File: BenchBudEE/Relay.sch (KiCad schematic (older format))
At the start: 11 parts

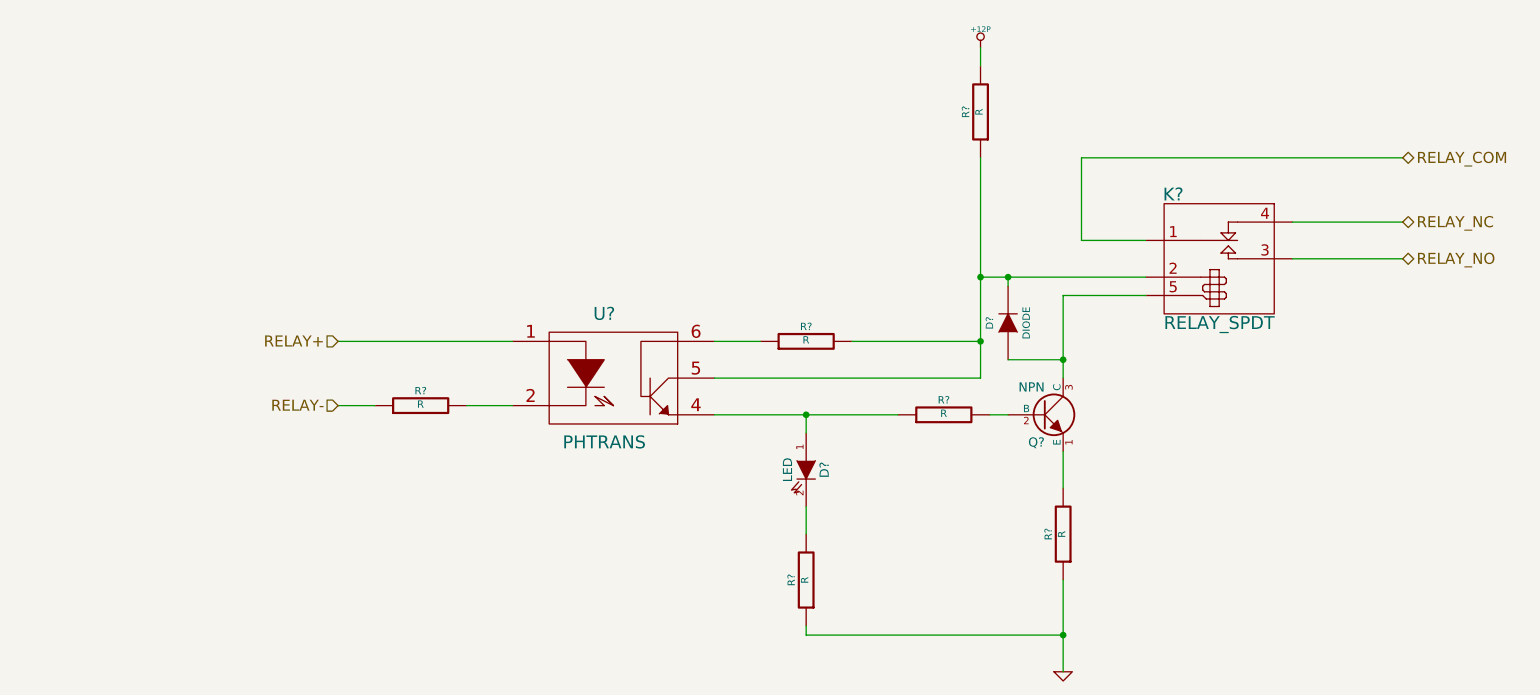
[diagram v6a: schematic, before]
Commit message: Parts added to relay module. Schematic tidied up.
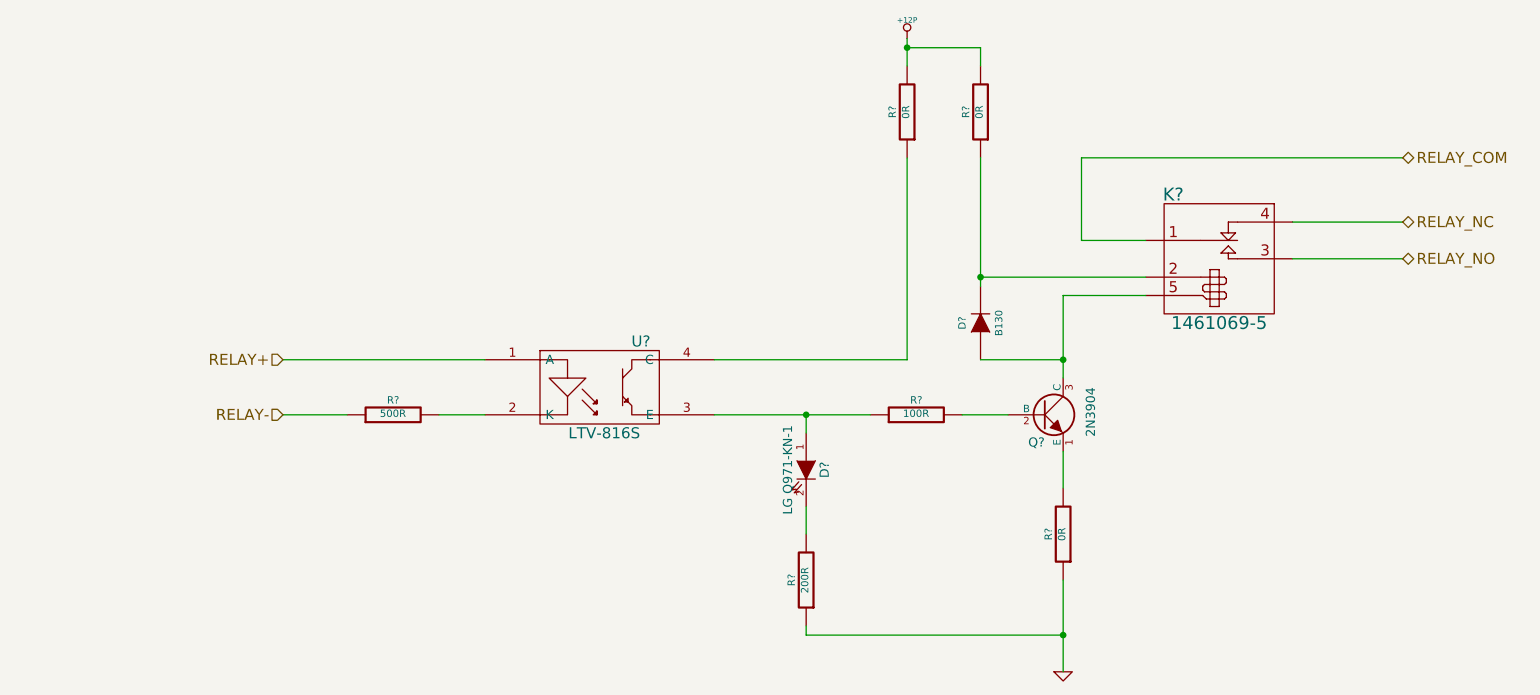
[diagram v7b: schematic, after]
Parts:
- removed R?: R, ~, symbol R
- removed U?: PHTRANS, ~, symbol PHTRANS
- added R?: 0R, ~, symbol R
- added U?: LTV-816S, symbol OPTO-TRANSISTOR4
- D?: value LED -> LG Q971-KN-1; Distributor (none) -> DigiKey; Distributor Part Link (none) -> http://www.digikey.com/product-detail/en/LG%20Q971-KN-1/475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; Distributor Part Number (none) -> 475-1409-1-ND; MFG Name (none) -> OSRAM Opto Semiconductors Inc; MFG Part Number (none) -> LG Q971-KN-1
- D?: value DIODE -> B130; Distributor (none) -> DigiKey; Distributor Part Link (none) -> http://www.digikey.com/product-detail/en/B130-13-F/B130-FDI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; Distributor Part Number (none) -> B130-FDICT-ND; MFG Name (none) -> Diodes Incorporated; MFG Part Number (none) -> B130-13-F
- K?: value RELAY_SPDT -> 1461069-5; Distributor (none) -> DigiKey; Distributor Part Link (none) -> http://www.digikey.com/product-detail/en/1461069-5/PB1321-N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; Distributor Part Number (none) -> PB1321-ND; MFG Name (none) -> TE Connectivity; MFG Part Number (none) -> 1461069-5
- Q?: value NPN -> 2N3904; Distributor (none) -> DigiKey; Distributor Part Link (none) -> http://www.digikey.com/product-detail/en/MMBT3904-7-F/MMBT3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; Distributor Part Number (none) -> MMBT3904-FDICT-ND; MFG Name (none) -> Diodes Incorporated; MFG Part Number (none) -> MMBT3904-7-F
- R?: value R -> 100R
- R? (x2): value R -> 0R
- R?: value R -> 200R
- R?: value R -> 500R
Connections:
- net +12P: now also R?.2
- net RELAY+: now also U?.1 (A)
- net at D?.1 (A), R?.1: now also U?.3 (E)
- net at R?.2: now also U?.2 (K)
- new net: R?.1, U?.4 (C)
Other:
- moved on the sheet: D?, R?
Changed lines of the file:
@@
 Sheet 2 9
 Title ""
-Date "8 feb 2014"
+Date "19 feb 2014"
 Rev ""
 Comp ""
@@
 Comment4 ""
 $EndDescr
-Text HLabel 3500 3550 0    60   Input ~ 0
+Text HLabel 3200 3650 0    60   Input ~ 0
 RELAY+
-Text HLabel 3500 3900 0    60   Input ~ 0
+Text HLabel 3200 3950 0    60   Input ~ 0
 RELAY-
 Text HLabel 9300 3100 2    60   BiDi ~ 0
@@
 RELAY_NC
 $Comp
-L PHTRANS U?
-U 1 1 52F2AEFF
-P 5000 3750
-F 0 "U?" H 4950 4100 70  0000 C CNN
-F 1 "PHTRANS" H 4950 3400 70  0000 C CNN
-F 2 "~" H 5000 3750 60  0000 C CNN
-F 3 "~" H 5000 3750 60  0000 C CNN
-	1    5000 3750
-	1    0    0    -1
-$EndComp
-$Comp
 L RELAY_SPDT K?
 U 1 1 52F29F66
 P 8300 3100
 F 0 "K?" H 8050 3450 70  0000 C CNN
-F 1 "RELAY_SPDT" H 8300 2750 70  0000 C CNN
+F 1 "1461069-5" H 8300 2750 70  0000 C CNN
 F 2 "~" H 8300 3250 60  0000 C CNN
-F 3 "~" H 8300 3250 60  0000 C CNN
+F 3 "http://media.digikey.com/pdf/Data%20Sheets/Tyco%20Electronics%20P%20B%20PDFs/ORWH.pdf" H 8300 3250 60  0001 C CNN
+F 4 "TE Connectivity" H 8300 3100 60  0001 C CNN "MFG Name"
+F 5 "1461069-5" H 8300 3100 60  0001 C CNN "MFG Part Number"
+F 6 "DigiKey" H 8300 3100 60  0001 C CNN "Distributor"
+F 7 "PB1321-ND" H 8300 3100 60  0001 C CNN "Distributor Part Number"
+F 8 "http://www.digikey.com/product-detail/en/1461069-5/PB1321-ND/3318145" H 8300 3100 60  0001 C CNN "Distributor Part Link"
 	1    8300 3100
 	1    0    0    -1
@@
 L R R?
 U 1 1 52F29F75
-P 6800 3950
-F 0 "R?" V 6880 3950 40  0000 C CNN
-F 1 "R" V 6807 3951 40  0000 C CNN
-F 2 "~" V 6730 3950 30  0000 C CNN
-F 3 "~" H 6800 3950 30  0000 C CNN
-	1    6800 3950
+P 6650 3950
+F 0 "R?" V 6730 3950 40  0000 C CNN
+F 1 "100R" V 6657 3951 40  0000 C CNN
+F 2 "~" V 6580 3950 30  0000 C CNN
+F 3 "~" H 6650 3950 30  0000 C CNN
+	1    6650 3950
 	0    -1   -1   0
 $EndComp
@@
 P 7350 3950
 F 0 "Q?" H 7350 3800 50  0000 R CNN
-F 1 "NPN" H 7350 4100 50  0000 R CNN
+F 1 "2N3904" V 7600 4100 50  0000 R CNN
 F 2 "~" H 7350 3950 60  0000 C CNN
-F 3 "~" H 7350 3950 60  0000 C CNN
+F 3 "http://www.diodes.com/datasheets/ds30036.pdf" H 7350 3950 60  0001 C CNN
+F 4 "Diodes Incorporated" H 7350 3950 60  0001 C CNN "MFG Name"
+F 5 "MMBT3904-7-F" H 7350 3950 60  0001 C CNN "MFG Part Number"
+F 6 "DigiKey" H 7350 3950 60  0001 C CNN "Distributor"
+F 7 "MMBT3904-FDICT-ND" H 7350 3950 60  0001 C CNN "Distributor Part Number"
+F 8 "http://www.digikey.com/product-detail/en/MMBT3904-7-F/MMBT3904-FDICT-ND/815727" H 7350 3950 60  0001 C CNN "Distributor Part Link"
 	1    7350 3950
 	1    0    0    -1
@@
 P 6050 4250
 F 0 "D?" H 6050 4350 50  0000 C CNN
-F 1 "LED" H 6050 4150 50  0000 C CNN
+F 1 "LG Q971-KN-1" H 6050 4150 50  0000 C CNN
 F 2 "~" H 6050 4250 60  0000 C CNN
-F 3 "~" H 6050 4250 60  0000 C CNN
+F 3 "http://catalog.osram-os.com/catalogue/catalogue.do;jsessionid=DE4D071D0D2758CC117C711BF848053E?act=downloadFile&favOid=0200000600005069000100b6" H 6050 4250 60  0001 C CNN
+F 4 "OSRAM Opto Semiconductors Inc" H 6050 4250 60  0001 C CNN "MFG Name"
+F 5 "LG Q971-KN-1" H 6050 4250 60  0001 C CNN "MFG Part Number"
+F 6 "DigiKey" H 6050 4250 60  0001 C CNN "Distributor"
+F 7 "475-1409-1-ND" H 6050 4250 60  0001 C CNN "Distributor Part Number"
+F 8 "http://www.digikey.com/product-detail/en/LG%20Q971-KN-1/475-1409-1-ND/1802597" H 6050 4250 60  0001 C CNN "Distributor Part Link"
 	1    6050 4250
 	0    1    1    0
@@
 P 7450 4600
 F 0 "R?" V 7530 4600 40  0000 C CNN
-F 1 "R" V 7457 4601 40  0000 C CNN
+F 1 "0R" V 7457 4601 40  0000 C CNN
 F 2 "~" V 7380 4600 30  0000 C CNN
 F 3 "~" H 7450 4600 30  0000 C CNN
@@
 P 6050 4850
 F 0 "R?" V 6130 4850 40  0000 C CNN
-F 1 "R" V 6057 4851 40  0000 C CNN
+F 1 "200R" V 6057 4851 40  0000 C CNN
 F 2 "~" V 5980 4850 30  0000 C CNN
 F 3 "~" H 6050 4850 30  0000 C CNN
@@
 $Comp
 L R R?
-U 1 1 52F2A0AD
-P 6050 3550
-F 0 "R?" V 6130 3550 40  0000 C CNN
-F 1 "R" V 6057 3551 40  0000 C CNN
-F 2 "~" V 5980 3550 30  0000 C CNN
-F 3 "~" H 6050 3550 30  0000 C CNN
-	1    6050 3550
-	0    -1   -1   0
-$EndComp
-$Comp
-L R R?
 U 1 1 52F2A0C7
 P 7000 2300
 F 0 "R?" V 7080 2300 40  0000 C CNN
-F 1 "R" V 7007 2301 40  0000 C CNN
+F 1 "0R" V 7007 2301 40  0000 C CNN
 F 2 "~" V 6930 2300 30  0000 C CNN
 F 3 "~" H 7000 2300 30  0000 C CNN
@@
 L R R?
 U 1 1 52F2A0F9
-P 3950 3900
-F 0 "R?" V 4030 3900 40  0000 C CNN
-F 1 "R" V 3957 3901 40  0000 C CNN
-F 2 "~" V 3880 3900 30  0000 C CNN
-F 3 "~" H 3950 3900 30  0000 C CNN
-	1    3950 3900
+P 3800 3950
+F 0 "R?" V 3880 3950 40  0000 C CNN
+F 1 "500R" V 3807 3951 40  0000 C CNN
+F 2 "~" V 3730 3950 30  0000 C CNN
+F 3 "~" H 3800 3950 30  0000 C CNN
+	1    3800 3950
 	0    -1   -1   0
 $EndComp
@@
 L +12P #PWR?
 U 1 1 52F2A164
-P 7000 1950
-F 0 "#PWR?" H 7000 1920 30  0001 C CNN
-F 1 "+12P" H 7000 2050 30  0000 C CNN
-F 2 "" H 7000 1950 60  0000 C CNN
-F 3 "" H 7000 1950 60  0000 C CNN
-	1    7000 1950
+P 6600 1900
+F 0 "#PWR?" H 6600 1870 30  0001 C CNN
+F 1 "+12P" H 6600 2000 30  0000 C CNN
+F 2 "" H 6600 1900 60  0000 C CNN
+F 3 "" H 6600 1900 60  0000 C CNN
+	1    6600 1900
 	1    0    0    -1
 $EndComp
@@
 L DIODE D?
 U 1 1 52F2A1DE
-P 7150 3450
-F 0 "D?" H 7150 3550 40  0000 C CNN
-F 1 "DIODE" H 7150 3350 40  0000 C CNN
-F 2 "~" H 7150 3450 60  0000 C CNN
-F 3 "~" H 7150 3450 60  0000 C CNN
-	1    7150 3450
+P 7000 3450
+F 0 "D?" H 7000 3550 40  0000 C CNN
+F 1 "B130" H 7000 3350 40  0000 C CNN
+F 2 "~" H 7000 3450 60  0000 C CNN
+F 3 "http://www.diodes.com/datasheets/ds13002.pdf" H 7000 3450 60  0001 C CNN
+F 4 "Diodes Incorporated" H 7000 3450 60  0001 C CNN "MFG Name"
+F 5 "B130-13-F" H 7000 3450 60  0001 C CNN "MFG Part Number"
+F 6 "DigiKey" H 7000 3450 60  0001 C CNN "Distributor"
+F 7 "B130-FDICT-ND" H 7000 3450 60  0001 C CNN "Distributor Part Number"
+F 8 "http://www.digikey.com/product-detail/en/B130-13-F/B130-FDICT-ND/815318" H 7000 3450 60  0001 C CNN "Distributor Part Link"
+	1    7000 3450
 	0    -1   -1   0
 $EndComp
@@
 	8700 2900 9300 2900
 Wire Wire Line
-	6050 3950 6550 3950
-Wire Wire Line
-	7050 3950 7150 3950
+	5550 3950 6400 3950
+Wire Wire Line
+	6900 3950 7150 3950
 Wire Wire Line
 	7450 4150 7450 4350
 Wire Wire Line
-	7450 3750 7450 3650
-Wire Wire Line
-	7450 3650 7450 3300
+	7450 3300 7450 3750
 Wire Wire Line
 	7450 3300 7900 3300
 Wire Wire Line
-	7900 3200 7150 3200
-Wire Wire Line
-	7150 3200 7000 3200
-Wire Wire Line
-	7000 2550 7000 3200
-Wire Wire Line
-	7000 3200 7000 3550
-Wire Wire Line
-	7000 3550 7000 3750
-Wire Wire Line
-	7450 4850 7450 5150
-Wire Wire Line
-	7450 5150 7450 5350
+	7000 3200 7900 3200
+Wire Wire Line
+	7450 4850 7450 5350
 Wire Wire Line
 	6050 4450 6050 4600
@@
 Connection ~ 7450 5150
 Wire Wire Line
-	7000 3750 5550 3750
-Connection ~ 7000 3200
-Wire Wire Line
-	5550 3550 5800 3550
-Wire Wire Line
-	6300 3550 7000 3550
-Connection ~ 7000 3550
-Wire Wire Line
-	4200 3900 4450 3900
-Wire Wire Line
-	3700 3900 3500 3900
-Wire Wire Line
-	3500 3550 4450 3550
+	4050 3950 4300 3950
+Wire Wire Line
+	3550 3950 3200 3950
 Wire Wire Line
 	7000 1950 7000 2050
@@
 	7550 3000 7900 3000
 Wire Wire Line
-	7150 3650 7450 3650
+	7000 3650 7450 3650
 Connection ~ 7450 3650
-Wire Wire Line
-	7150 3250 7150 3200
-Connection ~ 7150 3200
-Wire Wire Line
-	5550 3950 6050 3950
 Wire Wire Line
 	6050 4050 6050 3950
 Connection ~ 6050 3950
+$Comp
+L OPTO-TRANSISTOR4 U?
+U 1 1 53052DE1
+P 4950 3800
+F 0 "U?" H 5150 4050 60  0000 C CNN
+F 1 "LTV-816S" H 4950 3550 60  0000 C CNN
+F 2 "" H 4950 3800 60  0000 C CNN
+F 3 "http://optoelectronics.liteon.com/upload/download/DS-70-97-0013/P_100_LTV-816%20826%20846%20%28M,%20S,%20S-TA,%20S-TA1,%20S-TP%29%20Series.pdf" H 4950 3800 60  0001 C CNN
+F 4 "Lite-On Inc" H 4950 3800 60  0001 C CNN "MFG Name"
+F 5 "LTV-816S" H 4950 3800 60  0001 C CNN "MFG Part Number"
+F 6 "DigiKey" H 4950 3800 60  0001 C CNN "Distributor"
+F 7 "160-1361-5-ND" H 4950 3800 60  0001 C CNN "Distributor Part Number"
+F 8 "http://www.digikey.com/product-detail/en/LTV-816S/160-1361-5-ND/385831" H 4950 3800 60  0001 C CNN "Distributor Part Link"
+	1    4950 3800
+	1    0    0    -1
+$EndComp
+Wire Wire Line
+	3200 3650 4300 3650
+$Comp
+L R R?
+U 1 1 530533DD
+P 6600 2300
+F 0 "R?" V 6680 2300 40  0000 C CNN
+F 1 "0R" V 6607 2301 40  0000 C CNN
+F 2 "~" V 6530 2300 30  0000 C CNN
+F 3 "~" H 6600 2300 30  0000 C CNN
+	1    6600 2300
+	-1   0    0    1
+$EndComp
+Wire Wire Line
+	7000 1950 6600 1950
+Wire Wire Line
+	6600 1900 6600 2050
+Connection ~ 6600 1950
+Wire Wire Line
+	7000 2550 7000 3250
+Wire Wire Line
+	5550 3650 6600 3650
+Wire Wire Line
+	6600 3650 6600 2550
+Connection ~ 7000 3200
 $EndSCHEMATC

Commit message: Design rules specified for layout.
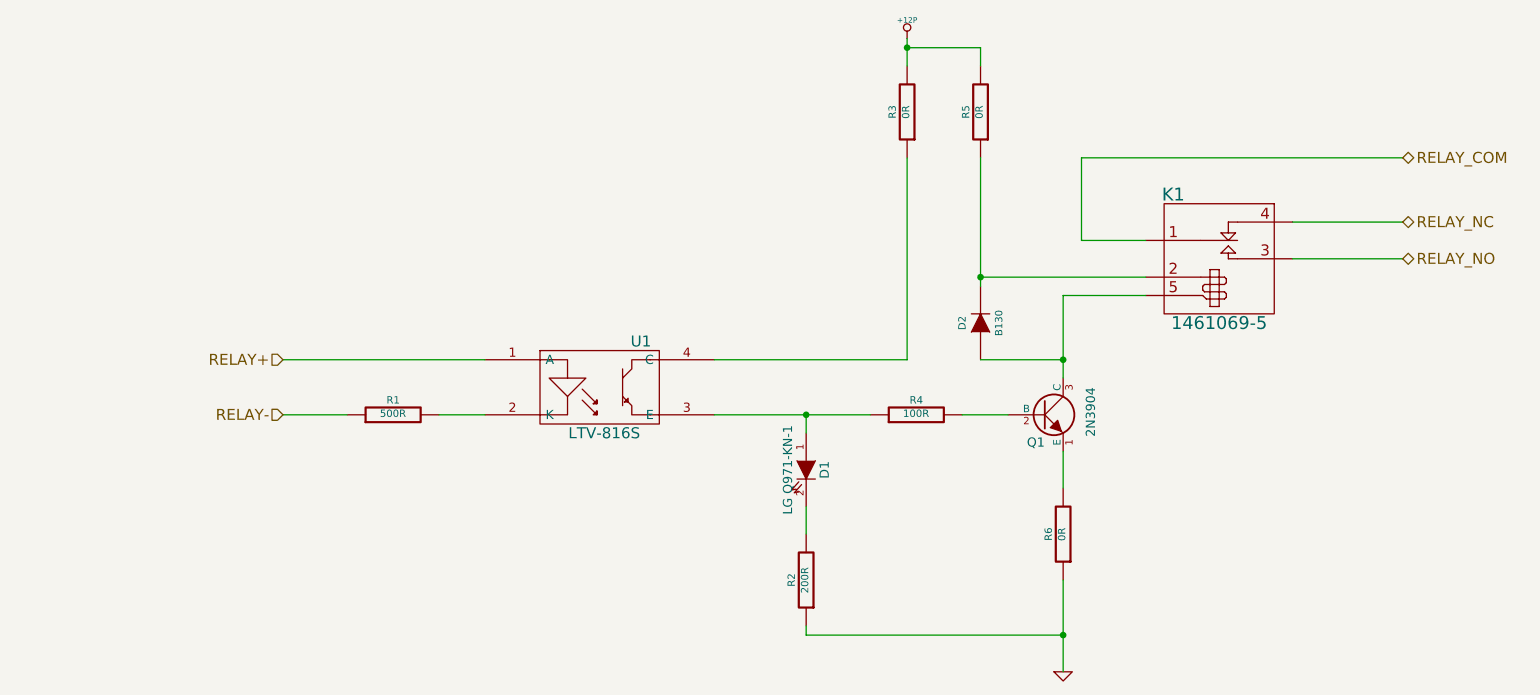
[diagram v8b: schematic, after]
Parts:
- gave numbers to parts that had none: 11
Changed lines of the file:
@@
 RELAY_NC
 $Comp
-L RELAY_SPDT K?
+L RELAY_SPDT K1
 U 1 1 52F29F66
 P 8300 3100
-F 0 "K?" H 8050 3450 70  0000 C CNN
+F 0 "K1" H 8050 3450 70  0000 C CNN
 F 1 "1461069-5" H 8300 2750 70  0000 C CNN
 F 2 "~" H 8300 3250 60  0000 C CNN
@@
 $EndComp
 $Comp
-L R R?
+L R R4
 U 1 1 52F29F75
 P 6650 3950
-F 0 "R?" V 6730 3950 40  0000 C CNN
+F 0 "R4" V 6730 3950 40  0000 C CNN
 F 1 "100R" V 6657 3951 40  0000 C CNN
 F 2 "~" V 6580 3950 30  0000 C CNN
@@
 $EndComp
 $Comp
-L NPN Q?
+L NPN Q1
 U 1 1 52F29F84
 P 7350 3950
-F 0 "Q?" H 7350 3800 50  0000 R CNN
+F 0 "Q1" H 7350 3800 50  0000 R CNN
 F 1 "2N3904" V 7600 4100 50  0000 R CNN
 F 2 "~" H 7350 3950 60  0000 C CNN
@@
 $EndComp
 $Comp
-L LED D?
+L LED D1
 U 1 1 52F29F93
 P 6050 4250
-F 0 "D?" H 6050 4350 50  0000 C CNN
+F 0 "D1" H 6050 4350 50  0000 C CNN
 F 1 "LG Q971-KN-1" H 6050 4150 50  0000 C CNN
 F 2 "~" H 6050 4250 60  0000 C CNN
@@
 RELAY_COM
 $Comp
-L R R?
+L R R6
 U 1 1 52F2A010
 P 7450 4600
-F 0 "R?" V 7530 4600 40  0000 C CNN
+F 0 "R6" V 7530 4600 40  0000 C CNN
 F 1 "0R" V 7457 4601 40  0000 C CNN
 F 2 "~" V 7380 4600 30  0000 C CNN
@@
 $EndComp
 $Comp
-L GND #PWR?
+L GND #PWR2
 U 1 1 52F2A023
 P 7450 5350
-F 0 "#PWR?" H 7450 5350 30  0001 C CNN
+F 0 "#PWR2" H 7450 5350 30  0001 C CNN
 F 1 "GND" H 7450 5280 30  0001 C CNN
 F 2 "" H 7450 5350 60  0000 C CNN
@@
 $EndComp
 $Comp
-L R R?
+L R R2
 U 1 1 52F2A068
 P 6050 4850
-F 0 "R?" V 6130 4850 40  0000 C CNN
+F 0 "R2" V 6130 4850 40  0000 C CNN
 F 1 "200R" V 6057 4851 40  0000 C CNN
 F 2 "~" V 5980 4850 30  0000 C CNN
@@
 $EndComp
 $Comp
-L R R?
+L R R5
 U 1 1 52F2A0C7
 P 7000 2300
-F 0 "R?" V 7080 2300 40  0000 C CNN
+F 0 "R5" V 7080 2300 40  0000 C CNN
 F 1 "0R" V 7007 2301 40  0000 C CNN
 F 2 "~" V 6930 2300 30  0000 C CNN
@@
 $EndComp
 $Comp
-L R R?
+L R R1
 U 1 1 52F2A0F9
 P 3800 3950
-F 0 "R?" V 3880 3950 40  0000 C CNN
+F 0 "R1" V 3880 3950 40  0000 C CNN
 F 1 "500R" V 3807 3951 40  0000 C CNN
 F 2 "~" V 3730 3950 30  0000 C CNN
@@
 $EndComp
 $Comp
-L +12P #PWR?
+L +12P #PWR1
 U 1 1 52F2A164
 P 6600 1900
-F 0 "#PWR?" H 6600 1870 30  0001 C CNN
+F 0 "#PWR1" H 6600 1870 30  0001 C CNN
 F 1 "+12P" H 6600 2000 30  0000 C CNN
 F 2 "" H 6600 1900 60  0000 C CNN
@@
 $EndComp
 $Comp
-L DIODE D?
+L DIODE D2
 U 1 1 52F2A1DE
 P 7000 3450
-F 0 "D?" H 7000 3550 40  0000 C CNN
+F 0 "D2" H 7000 3550 40  0000 C CNN
 F 1 "B130" H 7000 3350 40  0000 C CNN
 F 2 "~" H 7000 3450 60  0000 C CNN
@@
 Connection ~ 6050 3950
 $Comp
-L OPTO-TRANSISTOR4 U?
+L OPTO-TRANSISTOR4 U1
 U 1 1 53052DE1
 P 4950 3800
-F 0 "U?" H 5150 4050 60  0000 C CNN
+F 0 "U1" H 5150 4050 60  0000 C CNN
 F 1 "LTV-816S" H 4950 3550 60  0000 C CNN
 F 2 "" H 4950 3800 60  0000 C CNN
@@
 	3200 3650 4300 3650
 $Comp
-L R R?
+L R R3
 U 1 1 530533DD
 P 6600 2300
-F 0 "R?" V 6680 2300 40  0000 C CNN
+F 0 "R3" V 6680 2300 40  0000 C CNN
 F 1 "0R" V 6607 2301 40  0000 C CNN
 F 2 "~" V 6530 2300 30  0000 C CNN
